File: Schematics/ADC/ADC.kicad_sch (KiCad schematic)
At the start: 12 parts, among them J1 2-pin-header, J2 2-pin-header, J3 Conn_01x01, U1 ADS1115IDGST

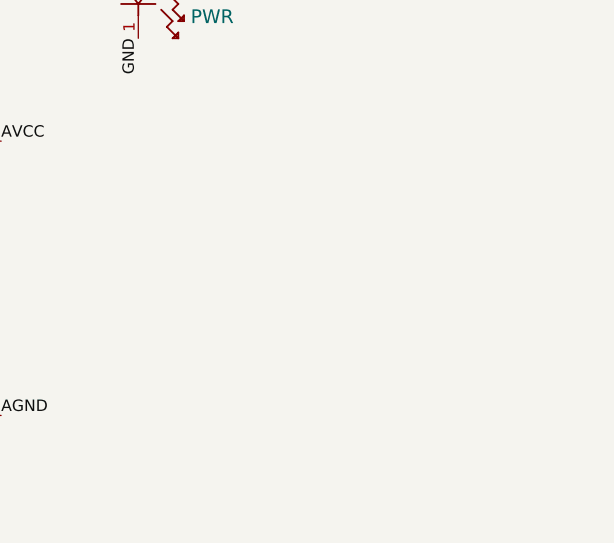
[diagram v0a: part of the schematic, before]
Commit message: updated schematic, layout and parts library
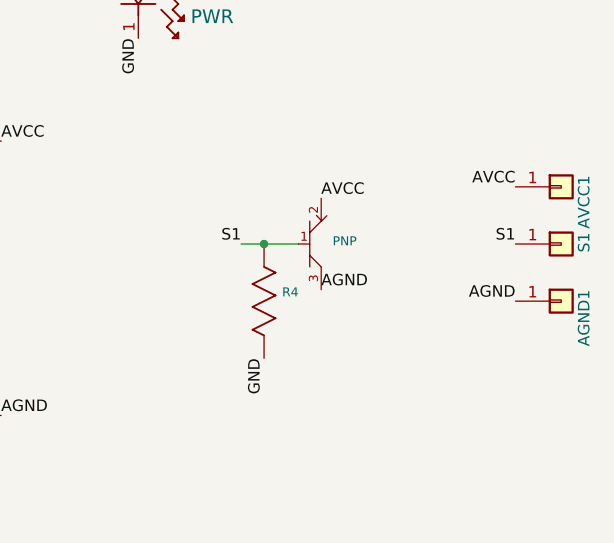
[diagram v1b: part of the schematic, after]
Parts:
- added AGND1, AVCC1, S1: Conn_01x01, pPSI:1 pin header, symbol Connector_Generic:Conn_01x01
- added R4: 10k, pPSI:10kohm resistor, symbol pPSI:10kohm-Resistor
- added T1: PNP, pPSI:PNP Transistor, symbol pPSI:PNP-Transistor
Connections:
- net AGND: now also AGND1.1 (Pin_1), T1.3
- net AVCC: now also AVCC1.1 (Pin_1), T1.2
- net GND: now also R4.1
- new net S1: R4.2, S1.1 (Pin_1), T1.1
